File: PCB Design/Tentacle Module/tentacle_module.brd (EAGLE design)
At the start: 101.6 x 30.5 mm, 57 parts, among them IC1 MC7805BDTRKG, IC2 UA78M33CKVU, T1 NTD5867NL, T2 NTD5867NL, T3 NTD5867NL, T4 NTD5867NL, U1 OKR-T/10-W12, X3 RJ45-8X, X4 RJ45-8X

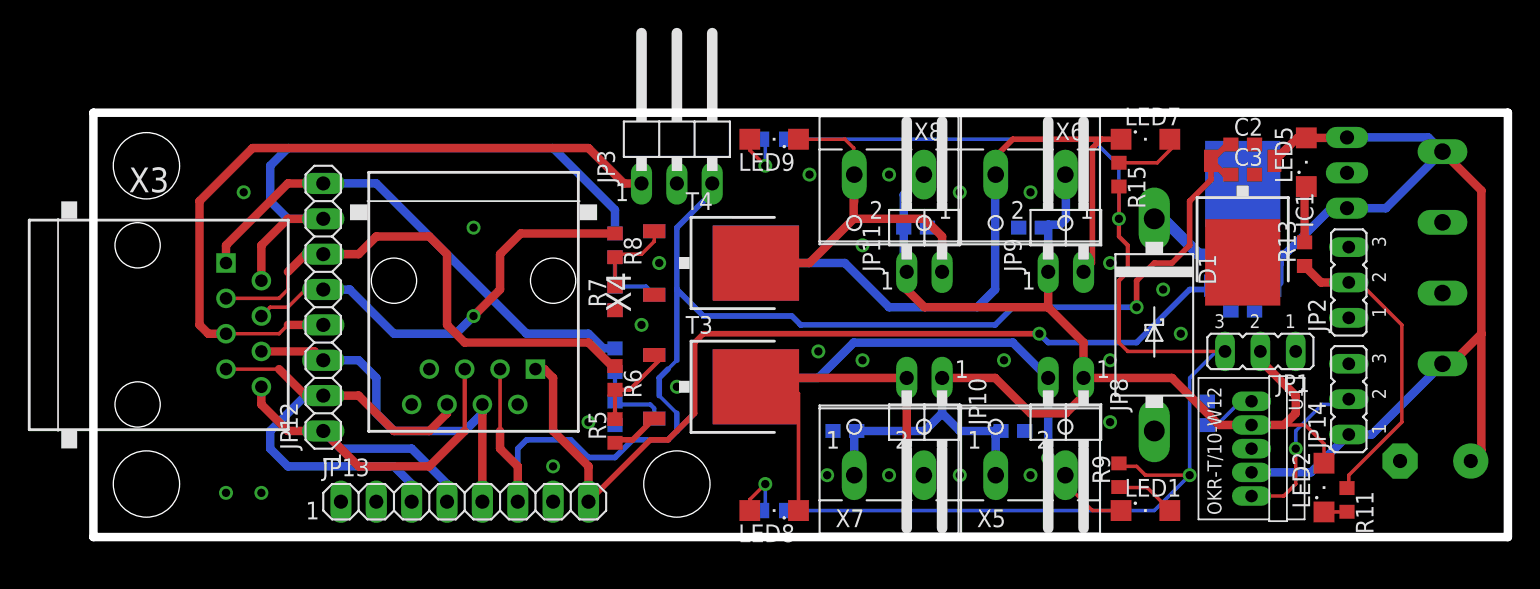
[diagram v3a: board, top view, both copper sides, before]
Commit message: Edited the silkscreen for Tentacle board
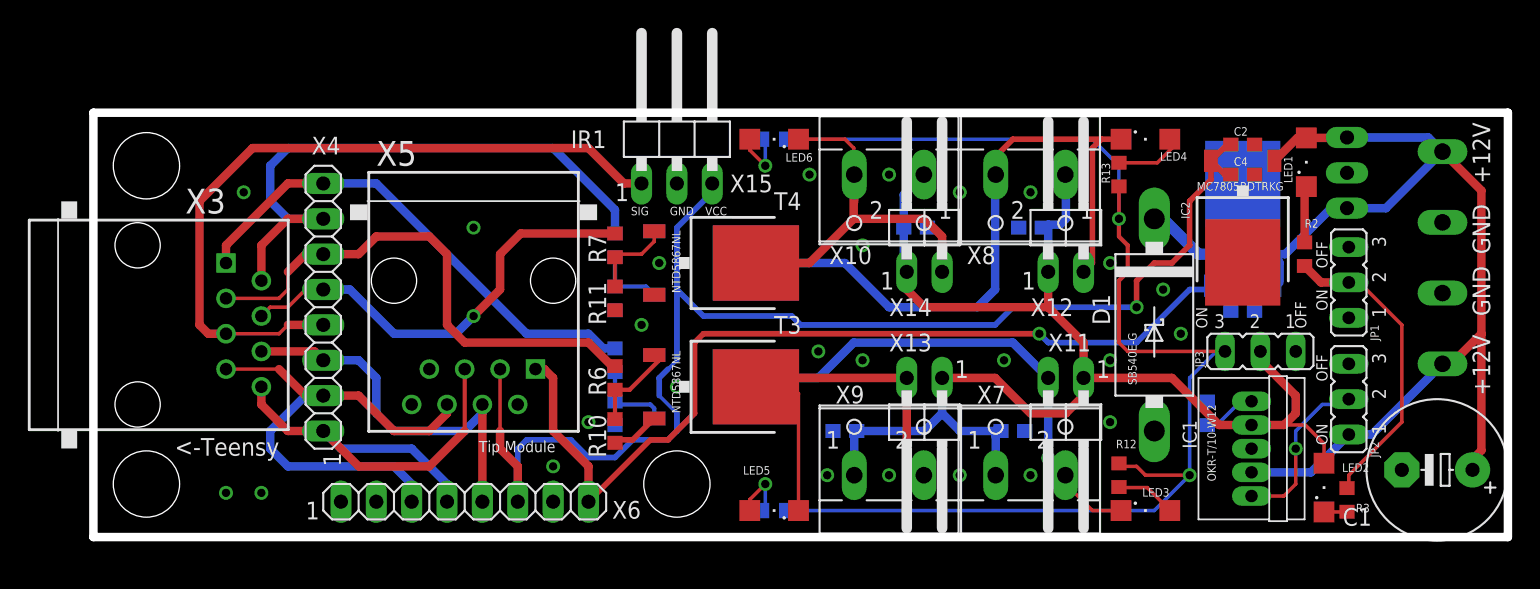
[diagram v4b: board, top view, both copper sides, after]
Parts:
- removed JP12, JP13: (no value), CBLA_Test_bed_Library:1X08
- removed JP14: (no value), jumper:JP2
- removed LED8: (no value), led:SML1206
- removed R17: 470, CBLA_Test_bed_Library:R0603
- removed U1: OKR-T/10-W12, CBLA_Test_bed_Library:OKR-C90
- added IC3: UA78M33CKVU, CBLA_Test_bed_Library:DPACK
- added LED3: (no value), led:SML1206
- added R12: 470, CBLA_Test_bed_Library:R0603
- added X10, X9: (no value), con-wago-500:W237-102
- added X15: (no value), CBLA_Test_bed_Library:1X03/90
- C3: value 100nF -> 10uF
- C4: value 10uF -> 100nF
- IC1: value MC7805BDTRKG -> OKR-T/10-W12; device CBLA_Test_bed_Library:DPACK_3 -> CBLA_Test_bed_Library:OKR-C90
- IC2: value UA78M33CKVU -> MC7805BDTRKG; device CBLA_Test_bed_Library:DPACK -> CBLA_Test_bed_Library:DPACK_3
- JP3: device CBLA_Test_bed_Library:1X03/90 -> jumper:JP2
- R1: value 4.7K -> 267
- R10: value 267 -> 4.7K
- R11, R9: value 470 -> 4.7K
- R2: value 4.7K -> 470
- R3: value 1K -> 470
- R5, R7: value 4.7K -> 1K
- R8: value 1K -> 4.7K
- X4: value RJ45-8X -> (none); device CBLA_Test_bed_Library:RJ45-NO-SHIELD -> CBLA_Test_bed_Library:1X08
- X5: value (none) -> RJ45-8X; device con-wago-500:W237-102 -> CBLA_Test_bed_Library:RJ45-NO-SHIELD
- X6: device con-wago-500:W237-102 -> CBLA_Test_bed_Library:1X08
- moved R11 54.5 mm to (37.5, 17.1), turned to 90 degrees
- moved R3 53.5 mm to (90.0, 2.67), flipped to the top
- moved R2 49.6 mm to (87.0, 20.3), flipped to the top
- moved X6 46.3 mm to (26.7, 2.54), turned to 0 degrees
- moved LED5 45.7 mm to (48.9, 1.91), turned to 180 degrees
- moved JP3 44.8 mm to (83.8, 13.3), turned to 180 degrees
- moved R10 42.6 mm to (37.5, 7.62), flipped to the top, turned to 90 degrees
- moved R1 42.5 mm to (80.0, 8.89), turned to 270 degrees
- moved X5 42.0 mm to (27.3, 18.4), turned to 180 degrees
- moved R9 38.4 mm to (37.5, 17.1), flipped to the bottom
- moved LED1 27.6 mm to (87.1, 26.9), turned to 90 degrees
- moved R15 24.9 mm to (48.9, 28.6), flipped to the bottom, turned to 180 degrees
- moved IC1 15.9 mm to (83.2, 6.35), turned to 270 degrees
- moved R13 14.5 mm to (73.7, 26.0), turned to 270 degrees
- moved R5 13.3 mm to (37.5, 21.0), flipped to the bottom, turned to 270 degrees
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- renumbered JP10 to X13, JP11 to X14, JP6 to X2, JP8 to X11, JP9 to X12, LED7 to LED4, LED9 to LED6, R16 to R14
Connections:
- net +12V: now also IC1.VIN, IC3.1, JP2.1, LED1.A; no longer IC1.1, JP14.1, LED5.A, U1.VIN
- net +3.3V: now also C3.1, IC3.3, X5.1, X6.8; no longer C4.1, IC2.3, JP13.8, X4.1
- net +5V: now also C4.1, IC2.3, X15.3, X5.3, X6.6; no longer C3.1, IC1.3, JP13.6, JP3.3, X4.3
- net +5V_HI-PWR: now also IC1.VOUT, JP3.2, X10.1, X9.1; no longer JP1.2, U1.VOUT, X5.1, X6.1
- net 5V_ENABLE: now also IC1.ON/OFF, JP2.2; no longer JP14.2, U1.ON/OFF
- net GND: now also IC1.GND, IC2.4, IC3.2, JP1.1, JP2.3, R11.1, R8.1, R9.1, X15.2, X5.2, X6.7; no longer IC1.4, IC2.2, JP13.7, JP14.3, JP2.1, JP3.2, R2.1, R5.1, R7.1, U1.GND, X4.2
- net IR1: now also X15.1, X4.4; no longer JP12.4, JP3.1
- net IR2: now also X4.3, X5.4, X6.5; no longer JP12.3, JP13.5, X4.4
- net N$1: now also R5.2, R9.2; no longer R2.2, R4.2
- net N$10: now also LED1.C, R2.2; no longer LED5.C, R13.2
- net N$12: now also R13.1; no longer R15.1
- net N$13: now also LED5.A; no longer LED8.A
- net N$14: now also R15.1; no longer R17.1
- net N$2: now also R10.2; no longer R5.2
- net N$3: now also R11.2; no longer R8.2
- net N$4: now also R4.2, R8.2; no longer R1.2, R3.2
- net N$5: now also LED3.A, R12.1; no longer LED1.A, R9.1
- net N$6: now also IC1.TRIM, R1.2; no longer R10.2, U1.TRIM
- net N$7: now also R3.2; no longer R11.2
- net PWM1: now also R4.1, X4.8; no longer JP12.8, R3.1
- net PWM2: now also R5.1, X4.7; no longer JP12.7, R4.1
- net PWM3: now also X4.6; no longer JP12.6
- net PWM4: now also R7.1, X4.5; no longer JP12.5, R8.1
- net PWR_LED_GND: now also JP1.2, R2.1, R3.1; no longer JP2.2, R11.1, R13.1
- net SCL: now also X4.2, X5.6, X6.3; no longer JP12.2, JP13.3, X4.6
- net SDA: now also X4.1, X5.5, X6.4; no longer JP12.1, JP13.4, X4.5
- net SMA1_OUT-: now also LED3.C, X7.2; no longer LED1.C, X5.2
- net SMA2_OUT-: now also X8.2; no longer X6.2
- net SMA3_OUT-: now also LED5.C, X9.2; no longer LED8.C, X7.2
- net SMA4_OUT-: now also X10.2; no longer X8.2
- net TEST_LED_V+: now also JP3.3, R12.2, R13.2; no longer JP1.3, R17.2, R9.2
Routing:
- net +12V: track 85.0 -> 85.6 mm
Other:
- board text added: "+12V"
- board text added: "<-Teensy"
- board text added: "GND"
- board text added: "IR1"
- board text added: "MC7805BDTRKG"
- board text added: "NTD5867NL"
- board text added: "OFF"
- board text added: "ON"
- board text added: "SB540E-G"
- board text added: "SIG"
- board text added: "Tip Module"
- board text added: "UA78M33CKVU"
- board text added: "VCC"

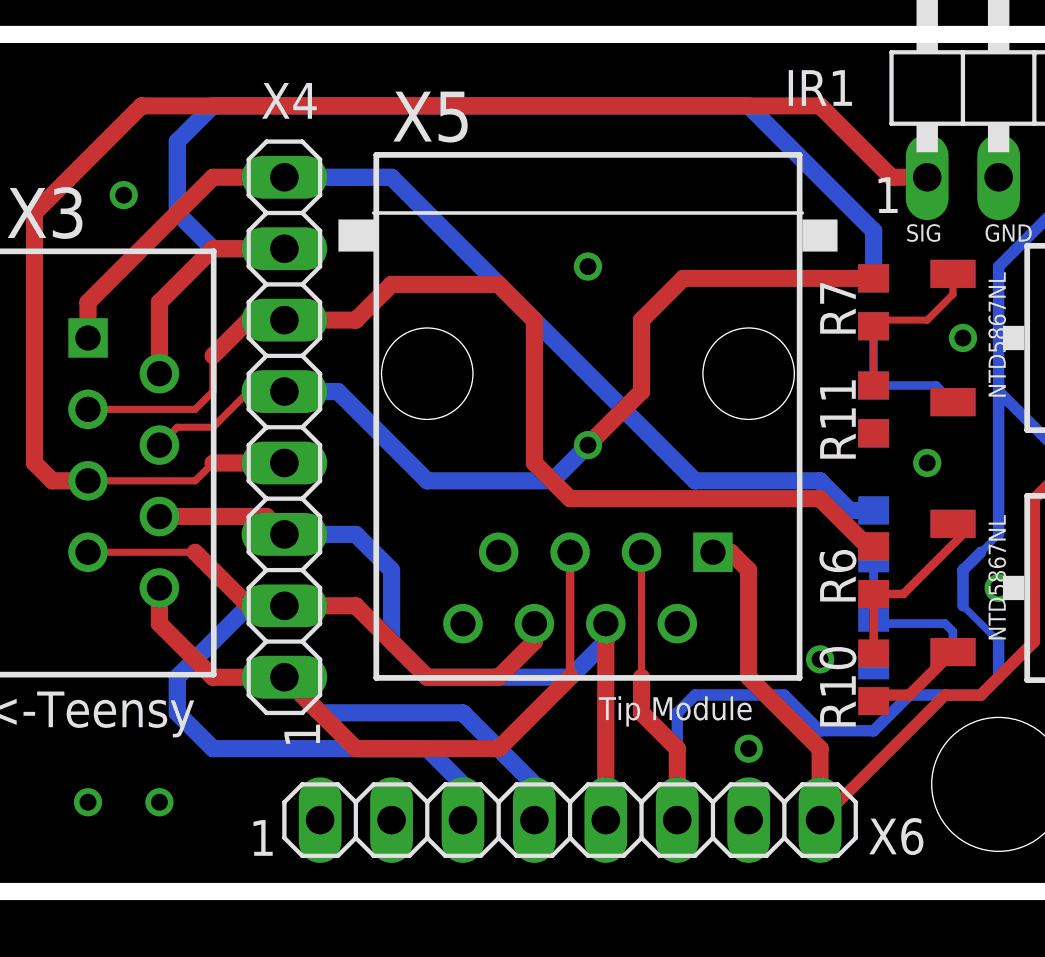
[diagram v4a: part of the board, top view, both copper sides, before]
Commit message: Swapped the SDA and SCL pins on the Tentacle tip connector
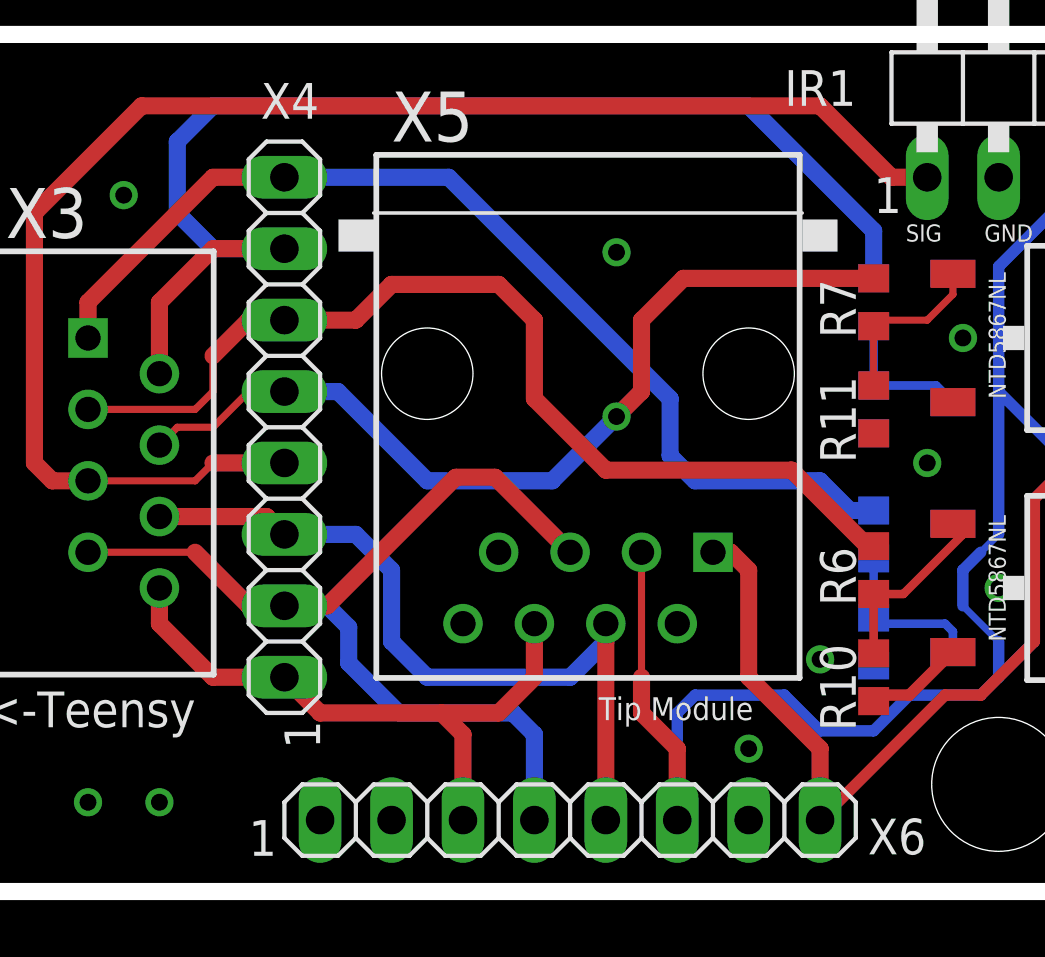
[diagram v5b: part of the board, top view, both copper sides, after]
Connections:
- net SCL: now also X5.5, X6.4; no longer X5.6, X6.3
- net SDA: now also X5.6, X6.3; no longer X5.5, X6.4
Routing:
- net SDA: track 35.0 -> 22.5 mm
- net SCL: track 37.5 -> 35.5 mm
- net PWM3: track 37.4 -> 36.0 mm
- net PWM1: track 36.0 -> 37.1 mm
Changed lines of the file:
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@@
 <wire x1="9.525" y1="20.955" x2="13.97" y2="25.4" width="0.6096" layer="1"/>
 <wire x1="13.97" y1="25.4" x2="16.51" y2="25.4" width="0.6096" layer="1"/>
-<wire x1="16.51" y1="25.4" x2="20.32" y2="25.4" width="0.6096" layer="16"/>
-<wire x1="20.32" y1="25.4" x2="31.115" y2="14.605" width="0.6096" layer="16"/>
+<wire x1="16.51" y1="25.4" x2="22.352" y2="25.4" width="0.6096" layer="16"/>
 <wire x1="31.115" y1="14.605" x2="35.56" y2="14.605" width="0.6096" layer="16"/>
 <wire x1="35.56" y1="14.605" x2="36.615" y2="13.55" width="0.6096" layer="16"/>
 <wire x1="36.615" y1="13.55" x2="37.465" y2="13.55" width="0.6096" layer="16"/>
+<wire x1="22.352" y1="25.4" x2="30.226" y2="17.526" width="0.6096" layer="16"/>
+<wire x1="30.226" y1="17.526" x2="30.226" y2="15.494" width="0.6096" layer="16"/>
+<wire x1="30.226" y1="15.494" x2="31.115" y2="14.605" width="0.6096" layer="16"/>
 </signal>
 <signal name="PWM2">
@@
 <wire x1="19.05" y1="20.32" x2="20.32" y2="21.59" width="0.6096" layer="1"/>
 <wire x1="20.32" y1="21.59" x2="24.13" y2="21.59" width="0.6096" layer="1"/>
-<wire x1="35.56" y1="13.97" x2="37.25" y2="12.28" width="0.6096" layer="1"/>
+<wire x1="34.544" y1="14.986" x2="37.25" y2="12.28" width="0.6096" layer="1"/>
 <wire x1="37.25" y1="12.28" x2="37.465" y2="12.28" width="0.6096" layer="1"/>
 <wire x1="24.13" y1="21.59" x2="25.4" y2="20.32" width="0.6096" layer="1"/>
-<wire x1="25.4" y1="20.32" x2="25.4" y2="15.24" width="0.6096" layer="1"/>
-<wire x1="25.4" y1="15.24" x2="26.67" y2="13.97" width="0.6096" layer="1"/>
-<wire x1="26.67" y1="13.97" x2="35.56" y2="13.97" width="0.6096" layer="1"/>
+<wire x1="25.4" y1="20.32" x2="25.4" y2="17.526" width="0.6096" layer="1"/>
+<wire x1="25.4" y1="17.526" x2="27.94" y2="14.986" width="0.6096" layer="1"/>
+<wire x1="27.94" y1="14.986" x2="34.544" y2="14.986" width="0.6096" layer="1"/>
 </signal>
 <signal name="PWM4">
@@
 <wire x1="18.415" y1="17.78" x2="21.59" y2="14.605" width="0.6096" layer="16"/>
 <wire x1="21.59" y1="14.605" x2="26.035" y2="14.605" width="0.6096" layer="16"/>
-<wire x1="26.035" y1="14.605" x2="27.305" y2="15.875" width="0.6096" layer="16"/>
-<via x="27.305" y="15.875" extent="1-16" drill="0.6"/>
-<wire x1="27.305" y1="15.875" x2="29.21" y2="17.78" width="0.6096" layer="1"/>
+<wire x1="26.035" y1="14.605" x2="28.321" y2="16.891" width="0.6096" layer="16"/>
+<via x="28.321" y="16.891" extent="1-16" drill="0.6"/>
+<wire x1="28.321" y1="16.891" x2="29.21" y2="17.78" width="0.6096" layer="1"/>
 <wire x1="29.21" y1="17.78" x2="29.21" y2="20.32" width="0.6096" layer="1"/>
 <wire x1="29.21" y1="20.32" x2="30.695" y2="21.805" width="0.6096" layer="1"/>
@@
 <signal name="SCL">
 <contactref element="X3" pad="7"/>
-<contactref element="X5" pad="6"/>
 <contactref element="X4" pad="2"/>
-<contactref element="X6" pad="3"/>
 <wire x1="16.51" y1="10.16" x2="15.24" y2="10.16" width="0.6096" layer="1"/>
 <wire x1="15.24" y1="10.16" x2="13.335" y2="12.065" width="0.6096" layer="1"/>
 <wire x1="13.335" y1="12.065" x2="9.525" y2="12.065" width="0.254" layer="1"/>
-<wire x1="16.51" y1="10.16" x2="15.24" y2="10.16" width="0.6096" layer="16"/>
-<wire x1="15.24" y1="10.16" x2="12.7" y2="7.62" width="0.6096" layer="16"/>
-<wire x1="12.7" y1="7.62" x2="12.7" y2="6.35" width="0.6096" layer="16"/>
-<wire x1="12.7" y1="6.35" x2="13.97" y2="5.08" width="0.6096" layer="16"/>
-<wire x1="13.97" y1="5.08" x2="21.59" y2="5.08" width="0.6096" layer="16"/>
-<wire x1="21.59" y1="5.08" x2="22.86" y2="3.81" width="0.6096" layer="16"/>
-<wire x1="22.86" y1="3.81" x2="22.86" y2="2.54" width="0.6096" layer="16"/>
-<wire x1="25.4" y1="9.525" x2="25.4" y2="8.89" width="0.6096" layer="1"/>
-<wire x1="25.4" y1="8.89" x2="24.13" y2="7.62" width="0.6096" layer="1"/>
-<wire x1="24.13" y1="7.62" x2="21.59" y2="7.62" width="0.6096" layer="1"/>
-<wire x1="21.59" y1="7.62" x2="19.05" y2="10.16" width="0.6096" layer="1"/>
-<wire x1="19.05" y1="10.16" x2="16.51" y2="10.16" width="0.6096" layer="1"/>
+<contactref element="X5" pad="5"/>
+<contactref element="X6" pad="4"/>
+<wire x1="26.67" y1="12.065" x2="24.003" y2="14.732" width="0.6096" layer="1"/>
+<wire x1="24.003" y1="14.732" x2="22.606" y2="14.732" width="0.6096" layer="1"/>
+<wire x1="22.606" y1="14.732" x2="18.034" y2="10.16" width="0.6096" layer="1"/>
+<wire x1="18.034" y1="10.16" x2="16.51" y2="10.16" width="0.6096" layer="1"/>
+<wire x1="25.4" y1="2.54" x2="25.4" y2="5.588" width="0.6096" layer="16"/>
+<wire x1="25.4" y1="5.588" x2="24.638" y2="6.35" width="0.6096" layer="16"/>
+<wire x1="24.638" y1="6.35" x2="20.574" y2="6.35" width="0.6096" layer="16"/>
+<wire x1="20.574" y1="6.35" x2="18.796" y2="8.128" width="0.6096" layer="16"/>
+<wire x1="18.796" y1="8.128" x2="18.796" y2="9.398" width="0.6096" layer="16"/>
+<wire x1="18.796" y1="9.398" x2="18.034" y2="10.16" width="0.6096" layer="16"/>
+<wire x1="18.034" y1="10.16" x2="16.51" y2="10.16" width="0.6096" layer="16"/>
 </signal>
 <signal name="SDA">
 <contactref element="X3" pad="8"/>
-<contactref element="X5" pad="5"/>
 <contactref element="X4" pad="1"/>
-<contactref element="X6" pad="4"/>
 <wire x1="12.065" y1="10.795" x2="12.065" y2="9.525" width="0.6096" layer="1"/>
 <wire x1="12.065" y1="9.525" x2="13.97" y2="7.62" width="0.6096" layer="1"/>
 <wire x1="13.97" y1="7.62" x2="16.51" y2="7.62" width="0.6096" layer="1"/>
-<wire x1="26.67" y1="12.065" x2="26.67" y2="7.62" width="0.3048" layer="1"/>
-<wire x1="26.67" y1="7.62" x2="24.13" y2="5.08" width="0.6096" layer="1"/>
-<wire x1="24.13" y1="5.08" x2="19.05" y2="5.08" width="0.6096" layer="1"/>
-<wire x1="19.05" y1="5.08" x2="16.51" y2="7.62" width="0.6096" layer="1"/>
-<wire x1="25.4" y1="2.54" x2="25.4" y2="3.81" width="0.6096" layer="16"/>
-<wire x1="25.4" y1="3.81" x2="22.86" y2="6.35" width="0.6096" layer="16"/>
-<wire x1="22.86" y1="6.35" x2="17.78" y2="6.35" width="0.6096" layer="16"/>
-<wire x1="17.78" y1="6.35" x2="16.51" y2="7.62" width="0.6096" layer="16"/>
+<contactref element="X5" pad="6"/>
+<contactref element="X6" pad="3"/>
+<wire x1="16.51" y1="7.62" x2="17.78" y2="6.35" width="0.6096" layer="1"/>
+<wire x1="17.78" y1="6.35" x2="22.098" y2="6.35" width="0.6096" layer="1"/>
+<wire x1="22.098" y1="6.35" x2="22.86" y2="5.588" width="0.6096" layer="1"/>
+<wire x1="22.86" y1="5.588" x2="22.86" y2="2.54" width="0.6096" layer="1"/>
+<wire x1="22.098" y1="6.35" x2="24.13" y2="6.35" width="0.6096" layer="1"/>
+<wire x1="24.13" y1="6.35" x2="25.4" y2="7.62" width="0.6096" layer="1"/>
+<wire x1="25.4" y1="7.62" x2="25.4" y2="9.525" width="0.6096" layer="1"/>
 </signal>
 <signal name="+3.3V">
@@
 <via x="9.525" y="3.175" extent="1-16" drill="0.6"/>
 <via x="10.795" y="24.765" extent="1-16" drill="0.6"/>
-<via x="27.305" y="22.225" extent="1-16" drill="0.6"/>
+<via x="28.321" y="22.733" extent="1-16" drill="0.6"/>
 <via x="51.435" y="26.035" extent="1-16" drill="0.6"/>
 <via x="73.025" y="8.255" extent="1-16" drill="0.6"/>
